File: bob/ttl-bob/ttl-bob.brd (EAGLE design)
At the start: 25.3 x 25.7 mm, 11 parts, among them U1 TXB0108

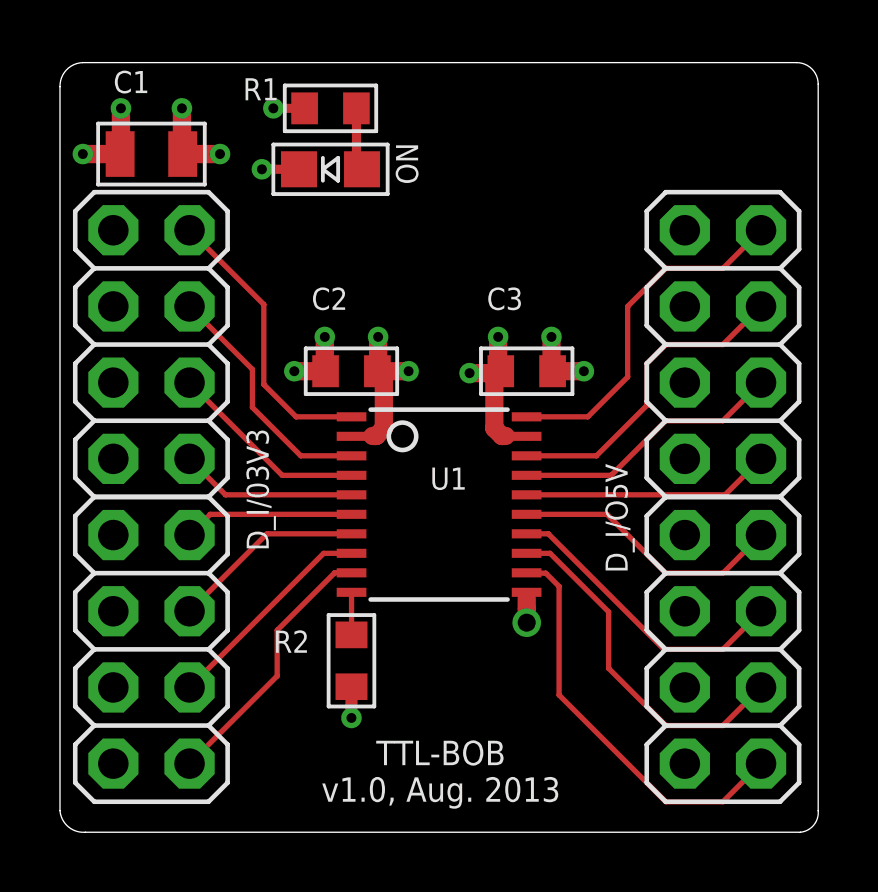
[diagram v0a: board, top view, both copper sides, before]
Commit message: Starting consolodating PuggleBoard library and adding part attributes containing DK part numbers.
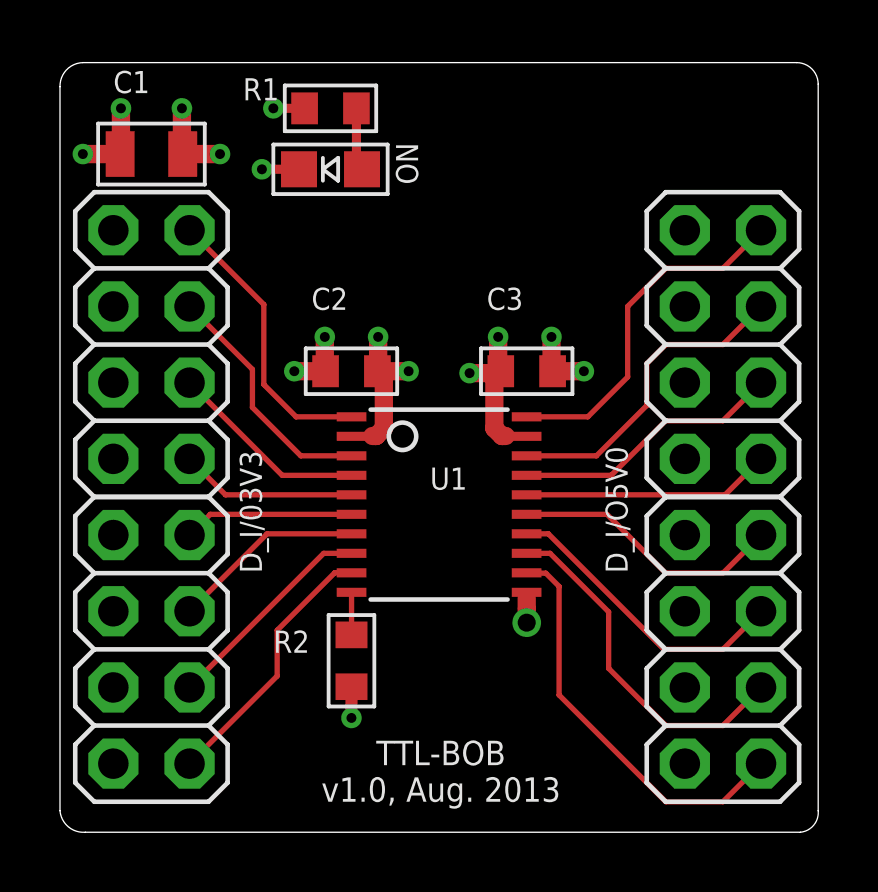
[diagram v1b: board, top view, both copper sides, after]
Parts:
- removed D_I/O5V: PINHD-2X8VERT, adafruit:2X08
- added D_I/O5V0: PINHD-2X8FEMALEVERT, puggleboard:2X08
- D_I/03V3: value PINHD-2X8VERT -> PINHD-2X8FEMALEVERT; device adafruit:2X08 -> puggleboard:2X08
- ON: value (none) -> LEDGREEN-CHIP0805
- U1: device adafruit:TSSOP20 -> puggleboard:TSSOP20
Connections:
- net GND: now also D_I/O5V0.11, D_I/O5V0.13, D_I/O5V0.15, D_I/O5V0.3, D_I/O5V0.5, D_I/O5V0.7, D_I/O5V0.9; no longer D_I/O5V.11, D_I/O5V.13, D_I/O5V.15, D_I/O5V.3, D_I/O5V.5, D_I/O5V.7, D_I/O5V.9
- net TTL0: now also D_I/O5V0.2; no longer D_I/O5V.2
- net TTL1: now also D_I/O5V0.4; no longer D_I/O5V.4
- net TTL2: now also D_I/O5V0.6; no longer D_I/O5V.6
- net TTL3: now also D_I/O5V0.8; no longer D_I/O5V.8
- net TTL4: now also D_I/O5V0.10; no longer D_I/O5V.10
- net TTL5: now also D_I/O5V0.12; no longer D_I/O5V.12
- net TTL6: now also D_I/O5V0.14; no longer D_I/O5V.14
- net TTL7: now also D_I/O5V0.16; no longer D_I/O5V.16
- net VCCB: now also D_I/O5V0.1; no longer D_I/O5V.1
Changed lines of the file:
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@@
 </autorouter>
 <elements>
-<element name="D_I/03V3" library="adafruit" package="2X08" value="PINHD-2X8VERT" x="3.048" y="11.176" smashed="yes" rot="R270">
-<attribute name="NAME" x="6.223" y="13.462" size="0.7366" layer="25" font="vector" ratio="10" rot="R270"/>
+<element name="D_I/03V3" library="puggleboard" package="2X08" value="PINHD-2X8FEMALEVERT" x="3.048" y="11.176" smashed="yes" rot="R270">
+<attribute name="NAME" x="6.731" y="8.636" size="0.7366" layer="25" font="vector" ratio="10" rot="R90"/>
+<attribute name="MN" value="Sullins" x="3.048" y="11.176" size="1.778" layer="27" rot="R270" display="off"/>
+<attribute name="DK" value="S7111-ND" x="3.048" y="11.176" size="1.778" layer="27" rot="R270" display="off"/>
+<attribute name="MPN" value="PPPC082LFBN-RC" x="3.048" y="11.176" size="1.778" layer="27" rot="R270" display="off"/>
 </element>
 <element name="C1" library="puggleboard" package="0805" value="10uF" x="3.048" y="22.606" smashed="yes">
 <attribute name="NAME" x="1.778" y="24.638" size="0.7366" layer="25" font="vector"/>
 <attribute name="VALUE" x="1.778" y="23.876" size="0.7366" layer="27" font="vector"/>
+<attribute name="DK" value="445-6797-1-ND" x="3.048" y="22.606" size="1.778" layer="27" display="off"/>
+<attribute name="MN" value="TDK Corp." x="3.048" y="22.606" size="1.778" layer="27" display="off"/>
+<attribute name="MPN" value="445-7644-1-ND" x="3.048" y="22.606" size="1.778" layer="27" display="off"/>
 </element>
 <element name="U$1" library="puggleboard" package="PB-LOGO" value="" x="19.812" y="10.16" rot="MR0"/>
-<element name="ON" library="puggleboard" package="CHIP-LED0805" value="" x="9.017" y="22.098" smashed="yes" rot="R90">
+<element name="ON" library="puggleboard" package="CHIP-LED0805" value="LEDGREEN-CHIP0805" x="9.017" y="22.098" smashed="yes" rot="R90">
 <attribute name="NAME" x="11.938" y="21.59" size="0.7366" layer="25" font="vector" rot="R90"/>
-<attribute name="VALUE" x="10.287" y="24.638" size="1.27" layer="27" rot="R180"/>
+<attribute name="MN" value="598-8170-107F" x="9.017" y="22.098" size="1.778" layer="27" rot="R90" display="off"/>
+<attribute name="DK" value="350-2044-1-ND" x="9.017" y="22.098" size="1.778" layer="27" rot="R90" display="off"/>
+<attribute name="MPN" value="Dialight" x="9.017" y="22.098" size="1.778" layer="27" rot="R90" display="off"/>
 </element>
 <element name="R1" library="puggleboard" package="0603" value="1k" x="9.017" y="24.13" smashed="yes">
@@
 <attribute name="VALUE" x="6.096" y="23.876" size="0.7366" layer="27" font="vector" ratio="10" align="center-left"/>
 </element>
-<element name="D_I/O5V" library="adafruit" package="2X08" value="PINHD-2X8VERT" x="22.098" y="11.176" smashed="yes" rot="R270">
+<element name="D_I/O5V0" library="puggleboard" package="2X08" value="PINHD-2X8FEMALEVERT" x="22.098" y="11.176" smashed="yes" rot="R270">
 <attribute name="NAME" x="18.923" y="8.636" size="0.7366" layer="25" font="vector" ratio="10" rot="R90"/>
-</element>
-<element name="U1" library="adafruit" package="TSSOP20" value="TXB0108" x="12.6365" y="10.922" smashed="yes" rot="R270">
+<attribute name="MN" value="Sullins" x="22.098" y="11.176" size="1.778" layer="27" rot="R270" display="off"/>
+<attribute name="DK" value="S7111-ND" x="22.098" y="11.176" size="1.778" layer="27" rot="R270" display="off"/>
+<attribute name="MPN" value="PPPC082LFBN-RC" x="22.098" y="11.176" size="1.778" layer="27" rot="R270" display="off"/>
+</element>
+<element name="U1" library="puggleboard" package="TSSOP20" value="TXB0108" x="12.6365" y="10.922" smashed="yes" rot="R270">
 <attribute name="NAME" x="12.3317" y="11.4196" size="0.7366" layer="25" font="vector" ratio="10"/>
 <attribute name="VALUE" x="10.922" y="5.588" size="0.7366" layer="27" font="vector" ratio="10"/>
+<attribute name="MN" value="Texas Instruments" x="12.6365" y="10.922" size="1.778" layer="27" rot="R270" display="off"/>
+<attribute name="DK" value="296-21527-1-ND " x="12.6365" y="10.922" size="1.778" layer="27" rot="R270" display="off"/>
+<attribute name="MPN" value="TXB0108PWR" x="12.6365" y="10.922" size="1.778" layer="27" rot="R270" display="off"/>
 </element>
 <element name="C2" library="puggleboard" package="0603" value="0.1uF" x="9.7155" y="15.367" smashed="yes" rot="R180">
@@
 <contactref element="ON" pad="C"/>
 <via x="6.731" y="22.098" extent="1-16" drill="0.3302"/>
-<contactref element="D_I/O5V" pad="15"/>
-<contactref element="D_I/O5V" pad="13"/>
-<contactref element="D_I/O5V" pad="11"/>
-<contactref element="D_I/O5V" pad="3"/>
-<contactref element="D_I/O5V" pad="5"/>
-<contactref element="D_I/O5V" pad="7"/>
-<contactref element="D_I/O5V" pad="9"/>
+<contactref element="D_I/O5V0" pad="15"/>
+<contactref element="D_I/O5V0" pad="13"/>
+<contactref element="D_I/O5V0" pad="11"/>
+<contactref element="D_I/O5V0" pad="3"/>
+<contactref element="D_I/O5V0" pad="5"/>
+<contactref element="D_I/O5V0" pad="7"/>
+<contactref element="D_I/O5V0" pad="9"/>
 <contactref element="U1" pad="11"/>
 <contactref element="C3" pad="2"/>
@@
 </signal>
 <signal name="TTL0">
-<contactref element="D_I/O5V" pad="2"/>
+<contactref element="D_I/O5V0" pad="2"/>
 <contactref element="U1" pad="20"/>
 <wire x1="23.368" y1="20.066" x2="22.098" y2="18.796" width="0.1778" layer="1"/>
@@
 </signal>
 <signal name="TTL1">
-<contactref element="D_I/O5V" pad="4"/>
+<contactref element="D_I/O5V0" pad="4"/>
 <contactref element="U1" pad="18"/>
 <wire x1="23.368" y1="17.526" x2="22.098" y2="16.256" width="0.1778" layer="1"/>
@@
 </signal>
 <signal name="TTL2">
-<contactref element="D_I/O5V" pad="6"/>
+<contactref element="D_I/O5V0" pad="6"/>
 <contactref element="U1" pad="17"/>
 <wire x1="23.368" y1="14.986" x2="22.098" y2="13.716" width="0.1778" layer="1"/>
@@
 </signal>
 <signal name="TTL3">
-<contactref element="D_I/O5V" pad="8"/>
+<contactref element="D_I/O5V0" pad="8"/>
 <contactref element="U1" pad="16"/>
 <wire x1="23.368" y1="12.446" x2="22.169" y2="11.247" width="0.1778" layer="1"/>
@@
 </signal>
 <signal name="TTL4">
-<contactref element="D_I/O5V" pad="10"/>
+<contactref element="D_I/O5V0" pad="10"/>
 <contactref element="U1" pad="15"/>
 <wire x1="23.368" y1="9.906" x2="22.098" y2="8.636" width="0.1778" layer="1"/>
@@
 </signal>
 <signal name="TTL5">
-<contactref element="D_I/O5V" pad="12"/>
+<contactref element="D_I/O5V0" pad="12"/>
 <contactref element="U1" pad="14"/>
 <wire x1="23.368" y1="7.366" x2="22.098" y2="6.096" width="0.1778" layer="1"/>
@@
 </signal>
 <signal name="TTL6">
-<contactref element="D_I/O5V" pad="14"/>
+<contactref element="D_I/O5V0" pad="14"/>
 <contactref element="U1" pad="13"/>
 <wire x1="23.368" y1="4.826" x2="22.098" y2="3.556" width="0.1778" layer="1"/>
@@
 </signal>
 <signal name="TTL7">
-<contactref element="D_I/O5V" pad="16"/>
+<contactref element="D_I/O5V0" pad="16"/>
 <contactref element="U1" pad="12"/>
 <wire x1="23.368" y1="2.286" x2="22.098" y2="1.016" width="0.1778" layer="1"/>
@@
 </signal>
 <signal name="VCCB" class="1">
-<contactref element="D_I/O5V" pad="1"/>
+<contactref element="D_I/O5V0" pad="1"/>
 <contactref element="U1" pad="19"/>
 <contactref element="C3" pad="1"/>
@@
 </signal>
 </signals>
-<errors>
-</errors>
 </board>
 </drawing>

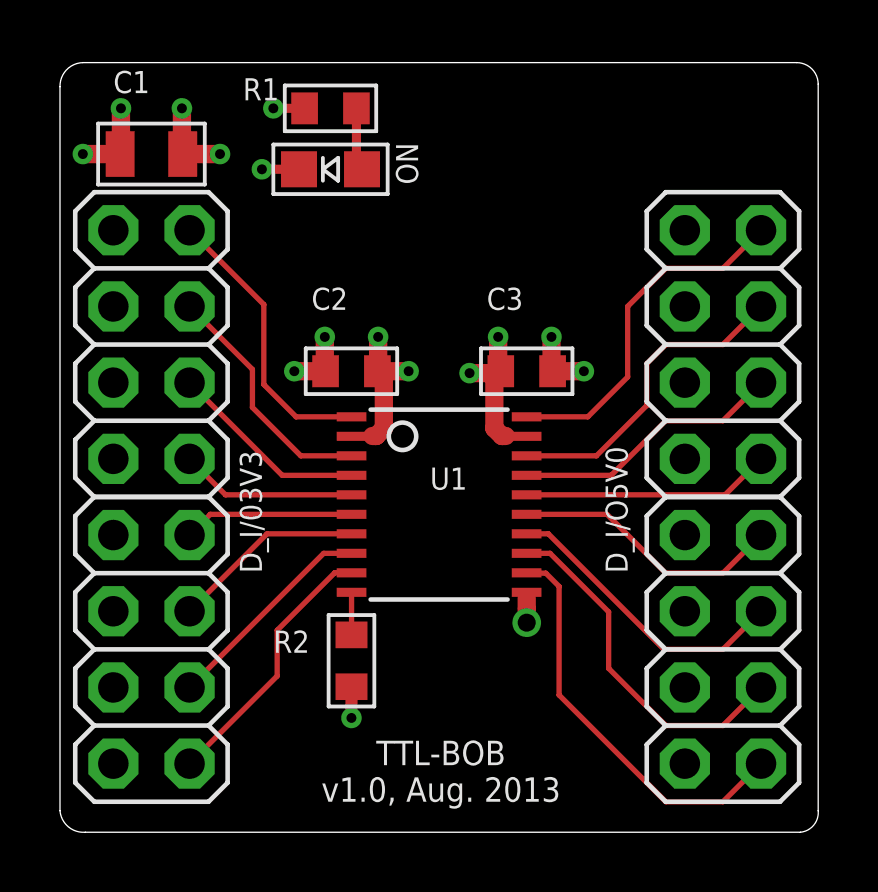
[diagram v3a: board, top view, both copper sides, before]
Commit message: For real this time. I have decided to use the BOM-AM.ULP parts managment program. I rebased the parts database to its format and started a global parts database in the ./parts folder.
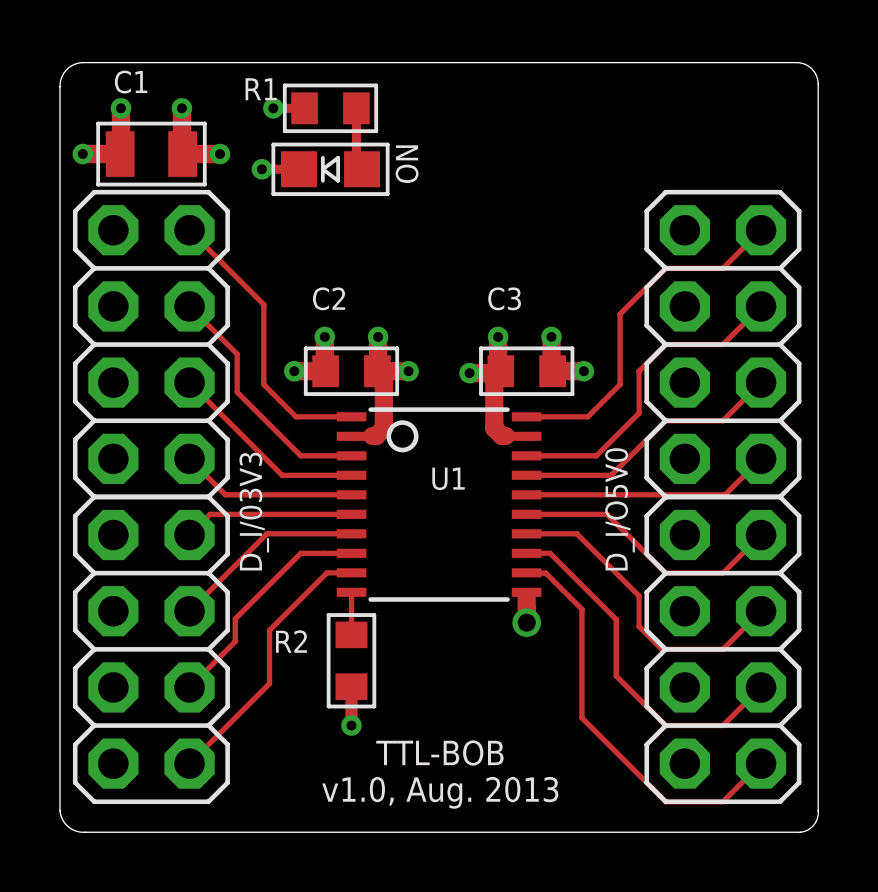
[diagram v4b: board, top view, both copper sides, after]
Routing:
- net TTL5: track 9.93 -> 10.5 mm
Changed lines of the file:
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@@
 <dimension x1="0" y1="25.654" x2="0" y2="0" x3="-4.318" y3="12.827" textsize="0.7366" layer="51" visible="yes"/>
 <rectangle x1="5.842" y1="3.81" x2="19.304" y2="6.35" layer="22"/>
-<dimension x1="25.273" y1="25.654" x2="0" y2="25.654" x3="12.6365" y3="30.226" textsize="0.7366" layer="51" visible="yes"/>
+<dimension x1="25.273" y1="25.654" x2="0" y2="25.654" x3="12.6365" y3="29.972" textsize="0.7366" layer="51" visible="yes"/>
 </plain>
 <attributes>
+<attribute name="PCB" value="TTL-BOB v1.0"/>
 </attributes>
 <variantdefs>
@@
 <contactref element="D_I/03V3" pad="14"/>
 <contactref element="U1" pad="8"/>
-<wire x1="4.318" y1="4.826" x2="8.789" y2="9.297" width="0.1778" layer="1"/>
+<wire x1="4.318" y1="4.826" x2="5.842" y2="6.35" width="0.1778" layer="1"/>
+<wire x1="5.842" y1="6.35" x2="5.842" y2="7.112" width="0.1778" layer="1"/>
+<wire x1="5.842" y1="7.112" x2="8.027" y2="9.297" width="0.1778" layer="1"/>
+<wire x1="8.027" y1="9.297" x2="8.789" y2="9.297" width="0.1778" layer="1"/>
 <wire x1="8.789" y1="9.297" x2="9.7187" y2="9.297" width="0.1778" layer="1"/>
 </signal>
@@
 <contactref element="D_I/03V3" pad="16"/>
 <contactref element="U1" pad="9"/>
-<wire x1="4.318" y1="2.286" x2="7.239" y2="5.207" width="0.1778" layer="1"/>
-<wire x1="7.239" y1="5.207" x2="7.239" y2="6.731" width="0.1778" layer="1"/>
-<wire x1="7.239" y1="6.731" x2="9.155" y2="8.647" width="0.1778" layer="1"/>
-<wire x1="9.155" y1="8.647" x2="9.7187" y2="8.647" width="0.1778" layer="1"/>
+<wire x1="4.318" y1="2.286" x2="6.985" y2="4.953" width="0.1778" layer="1"/>
+<wire x1="6.985" y1="4.953" x2="6.985" y2="6.731" width="0.1778" layer="1"/>
+<wire x1="6.985" y1="6.731" x2="8.901" y2="8.647" width="0.1778" layer="1"/>
+<wire x1="8.901" y1="8.647" x2="9.7187" y2="8.647" width="0.1778" layer="1"/>
 </signal>
 <signal name="VDRIVE1">
@@
 <contactref element="D_I/03V3" pad="4"/>
 <contactref element="U1" pad="3"/>
-<wire x1="4.318" y1="17.526" x2="6.4135" y2="15.4305" width="0.1778" layer="1"/>
-<wire x1="6.4135" y1="15.4305" x2="6.4135" y2="14.1605" width="0.1778" layer="1"/>
-<wire x1="6.4135" y1="14.1605" x2="8.027" y2="12.547" width="0.1778" layer="1"/>
+<wire x1="4.318" y1="17.526" x2="5.9055" y2="15.9385" width="0.1778" layer="1"/>
+<wire x1="5.9055" y1="15.9385" x2="5.9055" y2="14.6685" width="0.1778" layer="1"/>
+<wire x1="5.9055" y1="14.6685" x2="8.027" y2="12.547" width="0.1778" layer="1"/>
 <wire x1="8.027" y1="12.547" x2="9.7187" y2="12.547" width="0.1778" layer="1"/>
 </signal>
@@
 <wire x1="23.368" y1="20.066" x2="22.098" y2="18.796" width="0.1778" layer="1"/>
 <wire x1="22.098" y1="18.796" x2="20.193" y2="18.796" width="0.1778" layer="1"/>
-<wire x1="20.193" y1="18.796" x2="18.923" y2="17.526" width="0.1778" layer="1"/>
-<wire x1="18.923" y1="17.526" x2="18.923" y2="15.1765" width="0.1778" layer="1"/>
-<wire x1="18.923" y1="15.1765" x2="17.5935" y2="13.847" width="0.1778" layer="1"/>
+<wire x1="20.193" y1="18.796" x2="18.669" y2="17.272" width="0.1778" layer="1"/>
+<wire x1="18.669" y1="17.272" x2="18.669" y2="14.9225" width="0.1778" layer="1"/>
+<wire x1="18.669" y1="14.9225" x2="17.5935" y2="13.847" width="0.1778" layer="1"/>
 <wire x1="17.5935" y1="13.847" x2="15.5543" y2="13.847" width="0.1778" layer="1"/>
 </signal>
@@
 <wire x1="23.368" y1="17.526" x2="22.098" y2="16.256" width="0.1778" layer="1"/>
 <wire x1="22.098" y1="16.256" x2="20.193" y2="16.256" width="0.1778" layer="1"/>
-<wire x1="20.193" y1="16.256" x2="19.558" y2="15.621" width="0.1778" layer="1"/>
-<wire x1="19.558" y1="15.621" x2="19.558" y2="14.224" width="0.1778" layer="1"/>
-<wire x1="19.558" y1="14.224" x2="17.881" y2="12.547" width="0.1778" layer="1"/>
+<wire x1="20.193" y1="16.256" x2="19.304" y2="15.367" width="0.1778" layer="1"/>
+<wire x1="19.304" y1="15.367" x2="19.304" y2="13.97" width="0.1778" layer="1"/>
+<wire x1="19.304" y1="13.97" x2="17.881" y2="12.547" width="0.1778" layer="1"/>
 <wire x1="17.881" y1="12.547" x2="15.5543" y2="12.547" width="0.1778" layer="1"/>
 </signal>
@@
 <contactref element="U1" pad="14"/>
 <wire x1="23.368" y1="7.366" x2="22.098" y2="6.096" width="0.1778" layer="1"/>
-<wire x1="22.098" y1="6.096" x2="20.1295" y2="6.096" width="0.1778" layer="1"/>
-<wire x1="20.1295" y1="6.096" x2="16.2785" y2="9.947" width="0.1778" layer="1"/>
-<wire x1="16.2785" y1="9.947" x2="15.5543" y2="9.947" width="0.1778" layer="1"/>
+<wire x1="22.098" y1="6.096" x2="20.066" y2="6.096" width="0.1778" layer="1"/>
+<wire x1="20.066" y1="6.096" x2="19.304" y2="6.858" width="0.1778" layer="1"/>
+<wire x1="19.304" y1="6.858" x2="19.304" y2="7.874" width="0.1778" layer="1"/>
+<wire x1="19.304" y1="7.874" x2="17.231" y2="9.947" width="0.1778" layer="1"/>
+<wire x1="17.231" y1="9.947" x2="15.5543" y2="9.947" width="0.1778" layer="1"/>
 </signal>
 <signal name="TTL6">
@@
 <wire x1="23.368" y1="4.826" x2="22.098" y2="3.556" width="0.1778" layer="1"/>
 <wire x1="22.098" y1="3.556" x2="20.193" y2="3.556" width="0.1778" layer="1"/>
-<wire x1="20.193" y1="3.556" x2="18.288" y2="5.461" width="0.1778" layer="1"/>
-<wire x1="18.288" y1="5.461" x2="18.288" y2="7.34439375" width="0.1778" layer="1"/>
-<wire x1="18.288" y1="7.34439375" x2="16.33539375" y2="9.297" width="0.1778" layer="1"/>
+<wire x1="20.193" y1="3.556" x2="18.542" y2="5.207" width="0.1778" layer="1"/>
+<wire x1="18.542" y1="5.207" x2="18.542" y2="7.09039375" width="0.1778" layer="1"/>
+<wire x1="18.542" y1="7.09039375" x2="16.33539375" y2="9.297" width="0.1778" layer="1"/>
 <wire x1="16.33539375" y1="9.297" x2="15.5543" y2="9.297" width="0.1778" layer="1"/>
 </signal>
@@
 <wire x1="23.368" y1="2.286" x2="22.098" y2="1.016" width="0.1778" layer="1"/>
 <wire x1="22.098" y1="1.016" x2="20.193" y2="1.016" width="0.1778" layer="1"/>
-<wire x1="20.193" y1="1.016" x2="16.637" y2="4.572" width="0.1778" layer="1"/>
-<wire x1="16.637" y1="4.572" x2="16.637" y2="8.1915" width="0.1778" layer="1"/>
-<wire x1="16.637" y1="8.1915" x2="16.1925" y2="8.636" width="0.1778" layer="1"/>
+<wire x1="20.193" y1="1.016" x2="17.399" y2="3.81" width="0.1778" layer="1"/>
+<wire x1="17.399" y1="3.81" x2="17.399" y2="7.4295" width="0.1778" layer="1"/>
+<wire x1="17.399" y1="7.4295" x2="16.1925" y2="8.636" width="0.1778" layer="1"/>
 <wire x1="16.1925" y1="8.636" x2="15.5653" y2="8.636" width="0.1778" layer="1"/>
 <wire x1="15.5653" y1="8.636" x2="15.5543" y2="8.647" width="0.1778" layer="1"/>
@@
 <wire x1="10.6045" y1="15.367" x2="10.5791" y2="15.367" width="0.6096" layer="1"/>
 <wire x1="10.6045" y1="16.51" x2="10.6045" y2="15.367" width="0.6096" layer="1"/>
-<via x="9.7155" y="3.81" extent="1-16" drill="0.3302"/>
-<wire x1="9.7155" y1="4.8514" x2="9.7155" y2="3.81" width="0.4064" layer="1"/>
+<via x="9.7155" y="3.556" extent="1-16" drill="0.3302"/>
+<wire x1="9.7155" y1="4.8514" x2="9.7155" y2="3.556" width="0.4064" layer="1"/>
 <contactref element="R1" pad="1"/>
 <via x="7.112" y="24.13" extent="1-16" drill="0.3302"/>

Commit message: Finished BOMs (and integrated parts into database) for all the BOBs. Now must do for the main board. Will take a while.
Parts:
- ON: value LEDGREEN-CHIP0805 -> LEDGREEN_0805
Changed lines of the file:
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@@
 </element>
 <element name="U$1" library="puggleboard" package="PB-LOGO" value="" x="19.812" y="10.16" rot="MR0"/>
-<element name="ON" library="puggleboard" package="CHIP-LED0805" value="LEDGREEN-CHIP0805" x="9.017" y="22.098" smashed="yes" rot="R90">
+<element name="ON" library="puggleboard" package="CHIP-LED0805" value="LEDGREEN_0805" x="9.017" y="22.098" smashed="yes" rot="R90">
 <attribute name="NAME" x="11.938" y="21.59" size="0.7366" layer="25" font="vector" rot="R90"/>
 <attribute name="MN" value="598-8170-107F" x="9.017" y="22.098" size="1.778" layer="27" rot="R90" display="off"/>
